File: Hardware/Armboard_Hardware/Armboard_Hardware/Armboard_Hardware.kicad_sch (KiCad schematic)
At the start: 301 parts, among them J1 RJ45_LED_Shielded, J2 Conn_02x03_Counter_Clockwise, Q1 SI4156DY, Q10 SI4156DY, Q11 SI4156DY, Q12 SI4156DY, Q13 SI4156DY, Q14 SI4156DY, Q15 SI4156DY, Q16 SI4156DY, Q17 SI4156DY, Q18 SI4156DY, Q19 SI4156DY, Q2 SI4156DY, Q20 SI4156DY, Q21 SI4156DY, Q22 SI4156DY, Q23 SI4156DY, Q24 SI4156DY, Q25 SI4156DY, Q26 SI4156DY, Q27 SI4156DY, Q28 SI4156DY, Q29 BSS138, Q3 SI4156DY, Q30 SI4156DY, Q31 SI4156DY, Q32 SI4156DY, Q33 SI4156DY, Q34 SI4156DY, Q35 SI4156DY, Q36 SI4156DY, Q37 SI4156DY, Q38 BSS138, Q4 SI4156DY, Q5 SI4156DY, Q6 SI4156DY, Q7 SI4156DY, Q8 SI4156DY, Q9 SI4156DY, SW1 SW_Push_SPDT, SW10 SW_SPDT, SW2 SW_Push_SPDT, SW3 SW_Push_SPDT, SW4 SW_Push_SPDT, SW5 SW_Push_SPDT, SW6 SW_Push_SPDT, SW7 SW_Push_SPDT, SW8 SW_Push_SPDT, SW9 SW_Push_SPDT, U1 Teensy4.1_DEV-16771, U10 IRS2005S, U11 IRS2005S, U12 IRS2005S, U13 IRS2005S, U14 OKI, U15 IRS2005S, U16 IRS2005S, U17 IRS2005S, U18 IRS2005S, U19 IRS2005S, U2 IRS2005S, U20 IRS2005S, U21 74LVC2G04, U22 74LVC2G04, U23 74LVC2G04, U24 74LVC2G04, U25 74LVC2G04, U26 74LVC2G04, U27 74LVC2G04, U28 74LVC2G04, U29 74LVC2G04, U3 IRS2005S, U30 74HC148, U31 74HC148, U32 74HC00, U4 IRS2005S, U5 IRS2005S, U6 IRS2005S, U7 IRS2005S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

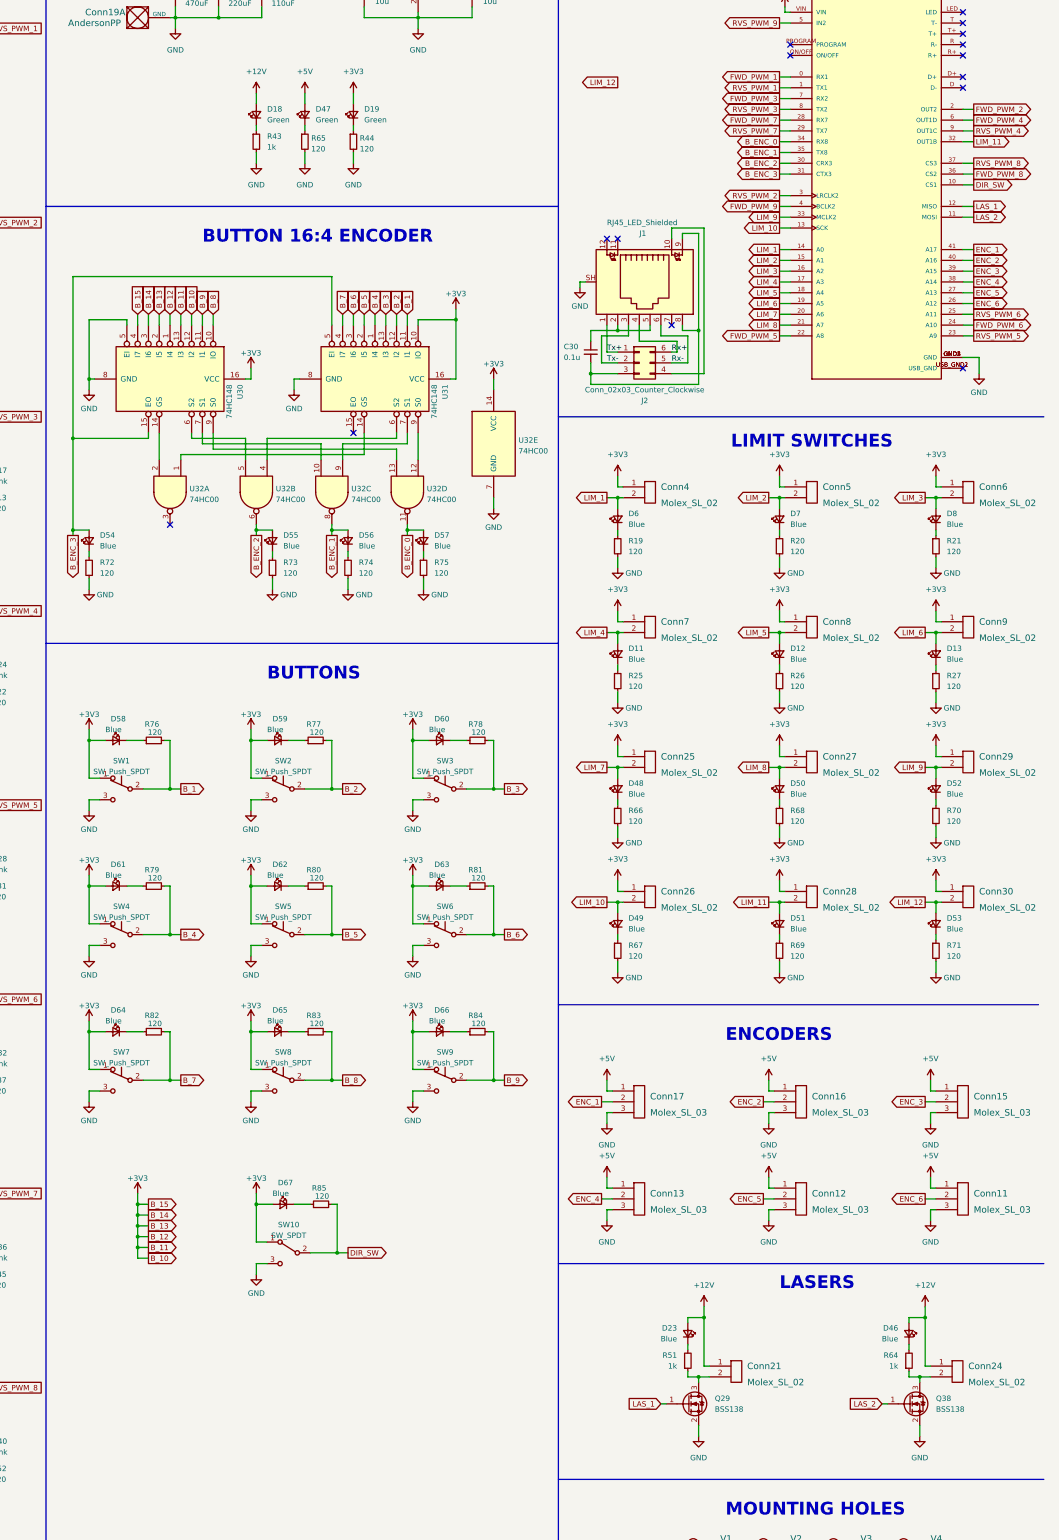
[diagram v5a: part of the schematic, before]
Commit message: Completed schematic
Combined laser toggles to save pin space on Teensy. Adjusted buttons from SPDT to SPST with pull-up resistors, to match standard.
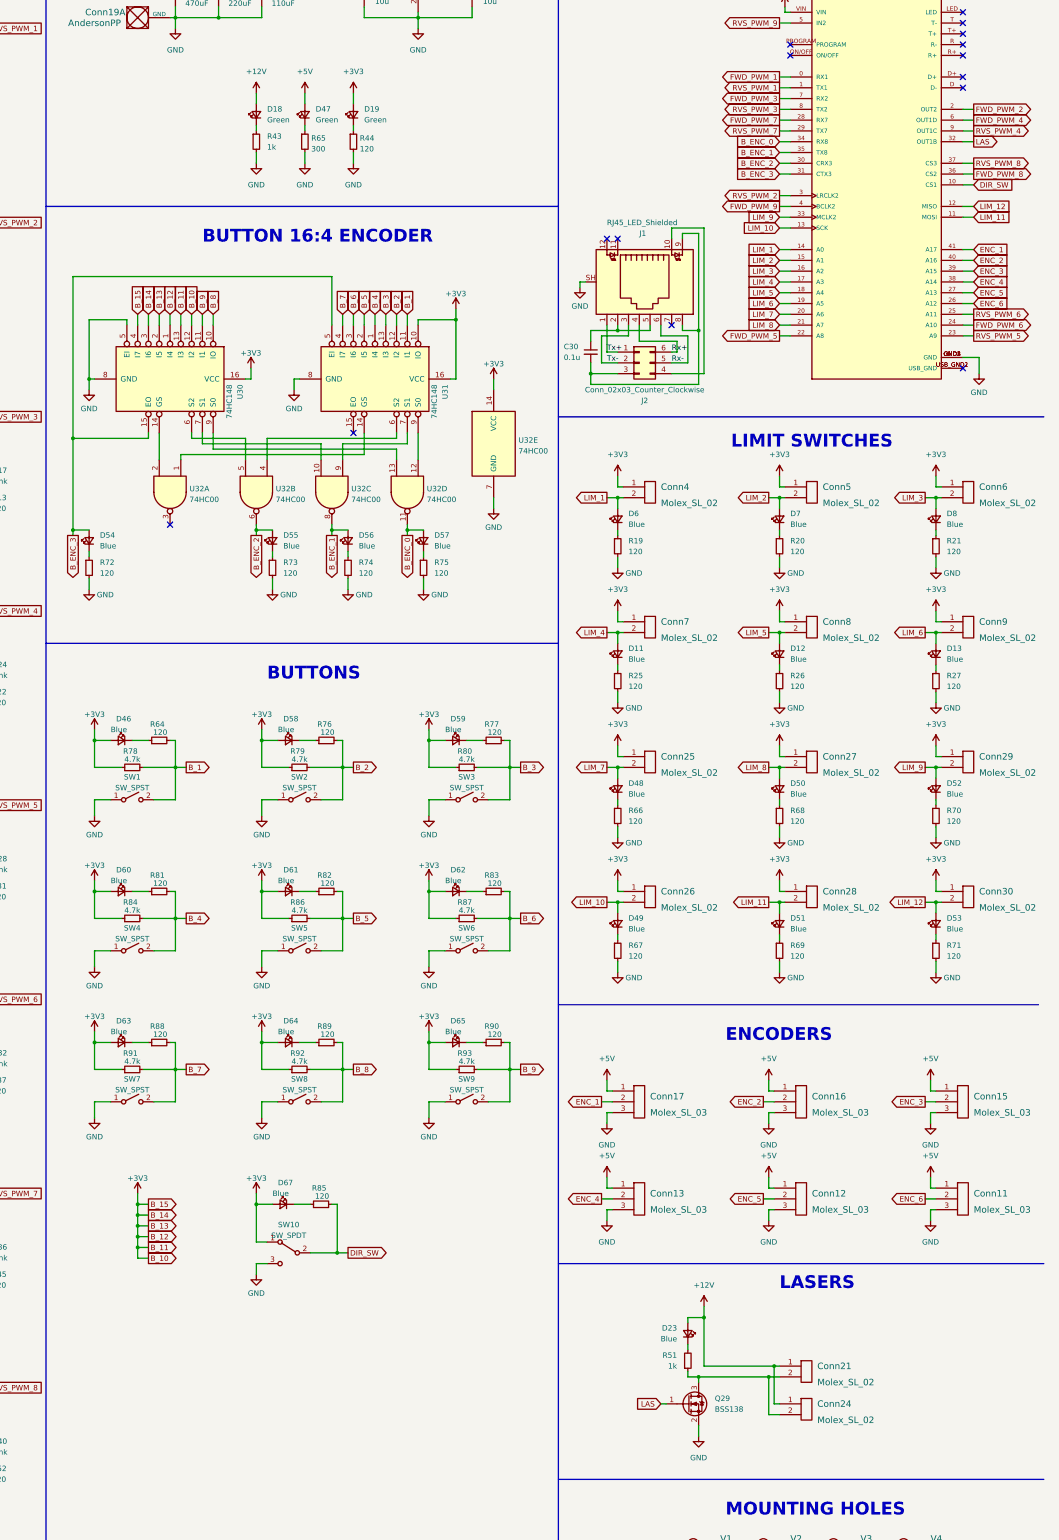
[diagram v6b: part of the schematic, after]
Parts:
- removed D46, D66: Blue, LED_SMD:LED_0603_1608Metric_Pad1.05x0.95mm_HandSolder, symbol Device:LED_Small
- removed Q38: BSS138, Package_TO_SOT_SMD:SOT-23, symbol Transistor_FET:BSS138
- removed R64: 1k, Resistor_SMD:R_0603_1608Metric_Pad0.98x0.95mm_HandSolder, symbol Device:R_Small
- removed SW1, SW2, SW3, SW4, SW5, SW6, SW7, SW8, SW9: SW_Push_SPDT, symbol Switch:SW_Push_SPDT
- added D58: Blue, LED_SMD:LED_0603_1608Metric_Pad1.05x0.95mm_HandSolder, symbol Device:LED_Small
- added R76, R88, R89, R90: 120, Resistor_SMD:R_0603_1608Metric_Pad0.98x0.95mm_HandSolder, symbol Device:R_Small
- added R86, R87, R91, R92, R93: 4.7k, Resistor_SMD:R_0603_1608Metric_Pad0.98x0.95mm_HandSolder, symbol Device:R_Small
- added SW1, SW2, SW3, SW4, SW5, SW6, SW7, SW8, SW9: SW_SPST, Button_Switch_SMD:SW_SPST_TL3305A, symbol Switch:SW_SPST
- R65: value 120 -> 300
- R78, R79, R80, R84: value 120 -> 4.7k
- SW10: footprint (none) -> Button_Switch_THT:SW_Slide_1P2T_CK_OS102011MS2Q
- renumbered D58 to D46, R76 to R64
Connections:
- net LAS_2 is gone; now on net LIM_11: U1.11 (MOSI)
- net +3V3: now also R78.1, R79.1, R80.1, R84.1, D58.2 (A), R86.1, R87.1, R91.1, R92.1, R93.1
- net B_1: now also R78.2, SW1.2 (B)
- net B_2: now also R79.2, R76.2, SW2.2 (B); no longer R77.2
- net B_3: now also R77.2, R80.2, SW3.2 (B); no longer R78.2
- net B_4: now also R81.2, R84.2, SW4.2 (B); no longer R79.2
- net B_5: now also R82.2, R86.2, SW5.2 (B); no longer R80.2
- net B_6: now also R83.2, R87.2, SW6.2 (B); no longer R81.2
- net B_7: now also R88.2, R91.2, SW7.2 (B); no longer R82.2
- net B_8: now also R89.2, R92.2, SW8.2 (B); no longer R83.2
- net B_9: now also R90.2, R93.2, SW9.2 (B); no longer R84.2
- net GND: now also SW1.1 (A), SW2.1 (A), SW3.1 (A), SW4.1 (A), SW5.1 (A), SW6.1 (A), SW7.1 (A), SW8.1 (A), SW9.1 (A)
- net LIM_11: no longer U1.32 (OUT1B)
- net LIM_12: now also U1.12 (MISO)
- net at Conn21.2, Q29.3 (D), R51.1: now also Conn24.2
- net at D65.1 (K): now also R90.1; no longer R83.1
- net at D64.1 (K): now also R89.1; no longer R82.1
- net at D60.1 (K): now also R81.1; no longer R78.1
- net at D61.1 (K): now also R82.1; no longer R79.1
- net at D62.1 (K): now also R83.1; no longer R80.1
- net at D63.1 (K): now also R88.1; no longer R81.1
- net LAS_1 renamed LAS
- net LAS: now also U1.32 (OUT1B); no longer U1.12 (MISO)
- new net: D58.1 (K), R76.1
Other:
- moved on the sheet: Conn21, Conn24, D46, R64

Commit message: Started layout
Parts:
- removed D54, D55, D56, D57: Blue, LED_SMD:LED_0603_1608Metric_Pad1.05x0.95mm_HandSolder, symbol Device:LED_Small
- removed J2: Conn_02x03_Counter_Clockwise, Connector_PinHeader_2.00mm:PinHeader_2x03_P2.00mm_Vertical, symbol Connector_Generic:Conn_02x03_Counter_Clockwise
- removed R72, R73, R74, R75: 120, Resistor_SMD:R_0603_1608Metric_Pad0.98x0.95mm_HandSolder, symbol Device:R_Small
- removed SW1, SW2, SW3, SW4, SW5, SW6, SW7, SW8, SW9: SW_SPST, Button_Switch_SMD:SW_SPST_TL3305A, symbol Switch:SW_SPST
- added D66, D68, D69, D70, D71, D72: Yellow, LED_SMD:LED_0603_1608Metric_Pad1.05x0.95mm_HandSolder, symbol Device:LED_Small
- added R94, R95, R96, R97, R98, R99: 300, Resistor_SMD:R_0603_1608Metric_Pad0.98x0.95mm_HandSolder, symbol Device:R_Small
- added SW1, SW2, SW3, SW4, SW5, SW6, SW7, SW8, SW9: SW_Push, Button_Switch_SMD:SW_SPST_TL3305A, symbol Switch:SW_Push
- C30: value 0.1u -> 0.1uF
- D1, D10, D14, D17, D2, D20, D24, D25, D28, D29, D32, D33, D36, D37, D40, D41, D44, D45: value Pink -> Orange
- D23: value Blue -> Orange
- J1: footprint MRDT_Connectors:RJ45_Teensy -> MRDT_Shields:Teensy_4_1_Ethernet
- U1: footprint MRDT_Shields:Teensy_4_1_Bare -> MRDT_Shields:Teensy_4_1
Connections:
- net B_1: now also SW1.2
- net B_2: now also SW2.2
- net B_3: now also SW3.2
- net B_4: now also SW4.2
- net B_5: now also SW5.2
- net B_6: now also SW6.2
- net B_7: now also SW7.2
- net B_8: now also SW8.2
- net B_9: now also SW9.2
- net ENC_1: now also D66.2 (A)
- net ENC_2: now also D68.2 (A)
- net ENC_3: now also D69.2 (A)
- net ENC_4: now also D70.2 (A)
- net ENC_5: now also D71.2 (A)
- net ENC_6: now also D72.2 (A)
- net GND: now also C30.2, J1.8, J1.9, R94.2, R95.2, R96.2, R97.2, R98.2, R99.2, SW1.1, SW2.1, SW3.1, SW4.1, SW5.1, SW6.1, SW7.1, SW8.1, SW9.1
- net Rx+: now also U1.R+
- net Rx-: now also U1.R (R-)
- net Tx+: now also U1.T+
- net Tx-: now also U1.T (T-)
- net LED: now reaches J1.10
- net LED: now also U1.LED
- new net: D72.1 (K), R99.1
- new net: D66.1 (K), R94.1
- new net: D70.1 (K), R97.1
- new net: D68.1 (K), R95.1
- new net: D71.1 (K), R98.1
- new net: D69.1 (K), R96.1
- no-connect marks 18 -> 13
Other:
- moved on the sheet: C30, Conn11, Conn12, Conn13, Conn15, Conn16, Conn17, Conn21, Conn24, D23, J1, Q29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

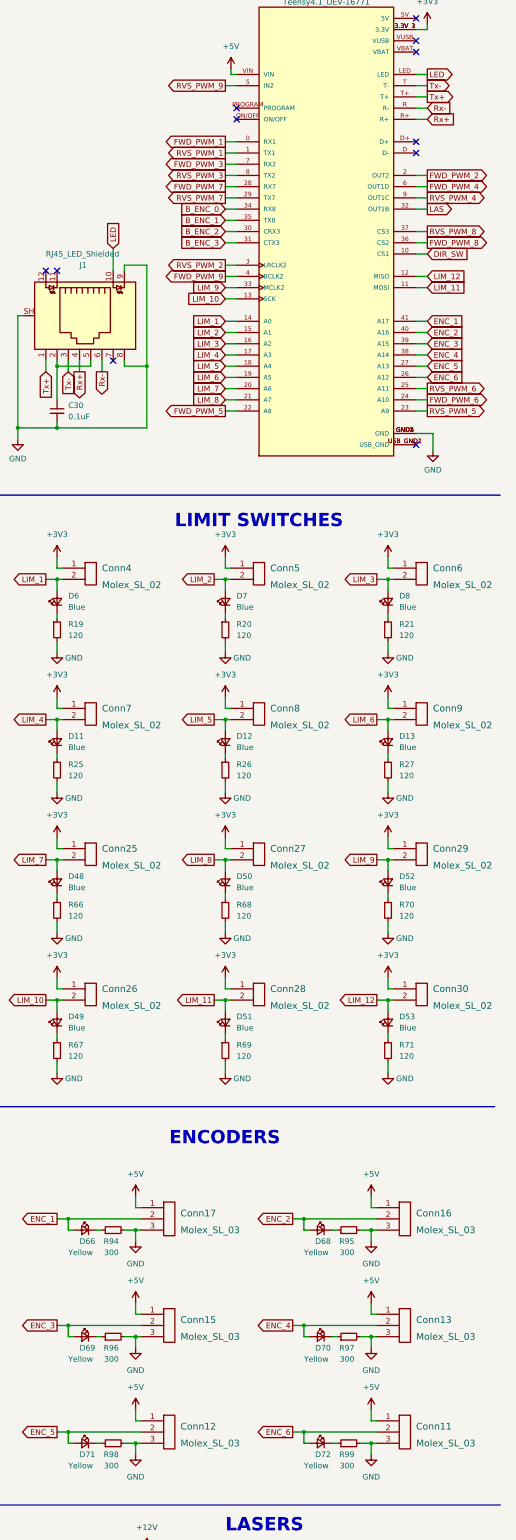
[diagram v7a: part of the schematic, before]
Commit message: Started routing traces
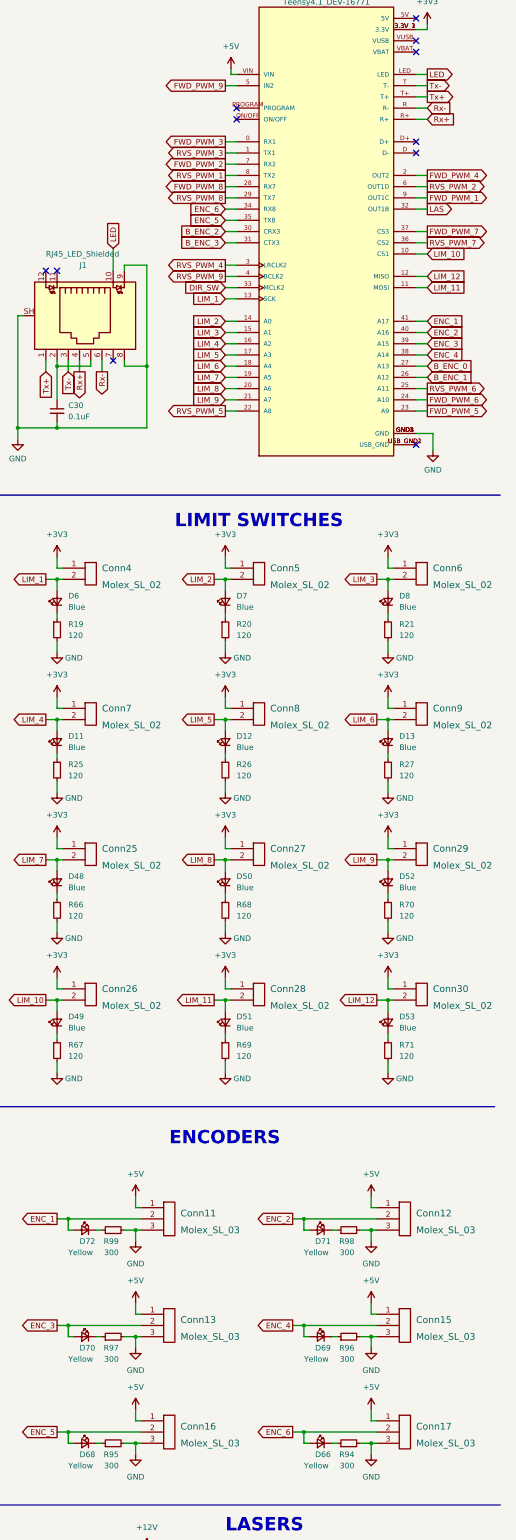
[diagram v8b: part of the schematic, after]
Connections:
- net B_ENC_0: now also U1.27 (A13); no longer U1.34 (RX8)
- net B_ENC_1: now also U1.26 (A12); no longer U1.35 (TX8)
- net DIR_SW: now also U1.33 (MCLK2); no longer U1.10 (CS1)
- net ENC_1: now also Conn11.2, D72.2 (A); no longer Conn17.2, D66.2 (A)
- net ENC_2: now also Conn12.2, D71.2 (A); no longer Conn16.2, D68.2 (A)
- net ENC_3: now also Conn13.2, D70.2 (A); no longer Conn15.2, D69.2 (A)
- net ENC_4: now also Conn15.2, D69.2 (A); no longer Conn13.2, D70.2 (A)
- net ENC_5: now also Conn16.2, D68.2 (A), U1.35 (TX8); no longer Conn12.2, D71.2 (A), U1.27 (A13)
- net ENC_6: now also Conn17.2, D66.2 (A), U1.34 (RX8); no longer Conn11.2, D72.2 (A), U1.26 (A12)
- net FWD_PWM_1: now also U1.9 (OUT1C); no longer U1.0 (RX1)
- net FWD_PWM_2: now also U1.7 (RX2); no longer U1.2 (OUT2)
- net FWD_PWM_3: now also U1.0 (RX1); no longer U1.7 (RX2)
- net FWD_PWM_4: now also U1.2 (OUT2); no longer U1.6 (OUT1D)
- net FWD_PWM_5: now also U1.23 (A9); no longer U1.22 (A8)
- net FWD_PWM_7: now also U1.37 (CS3); no longer U1.28 (RX7)
- net FWD_PWM_8: now also U1.28 (RX7); no longer U1.36 (CS2)
- net FWD_PWM_9: now also U1.5 (IN2); no longer U1.4 (BCLK2)
- net LIM_1: now also U1.13 (SCK); no longer U1.14 (A0)
- net LIM_10: now also U1.10 (CS1); no longer U1.13 (SCK)
- net LIM_2: now also U1.14 (A0); no longer U1.15 (A1)
- net LIM_3: now also U1.15 (A1); no longer U1.16 (A2)
- net LIM_4: now also U1.16 (A2); no longer U1.17 (A3)
- net LIM_5: now also U1.17 (A3); no longer U1.18 (A4)
- net LIM_6: now also U1.18 (A4); no longer U1.19 (A5)
- net LIM_7: now also U1.19 (A5); no longer U1.20 (A6)
- net LIM_8: now also U1.20 (A6); no longer U1.21 (A7)
- net LIM_9: now also U1.21 (A7); no longer U1.33 (MCLK2)
- net RVS_PWM_1: now also U1.8 (TX2); no longer U1.1 (TX1)
- net RVS_PWM_2: now also U1.6 (OUT1D); no longer U1.3 (LRCLK2)
- net RVS_PWM_3: now also U1.1 (TX1); no longer U1.8 (TX2)
- net RVS_PWM_4: now also U1.3 (LRCLK2); no longer U1.9 (OUT1C)
- net RVS_PWM_5: now also U1.22 (A8); no longer U1.23 (A9)
- net RVS_PWM_7: now also U1.36 (CS2); no longer U1.29 (TX7)
- net RVS_PWM_8: now also U1.29 (TX7); no longer U1.37 (CS3)
- net RVS_PWM_9: now also U1.4 (BCLK2); no longer U1.5 (IN2)
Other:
- moved on the sheet: Conn11, Conn12, Conn13, Conn15, Conn16, Conn17, D66, D68, D69, D70, D71, D72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
